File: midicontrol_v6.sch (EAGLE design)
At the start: 67 parts, among them SW1 EC12E_SW, U1 6N138S(TB), U2 PCA9634PW,112, U3 74HC595D, U4 ATMEGA328P-AN, Y1 CSTCE16M0V53-R0

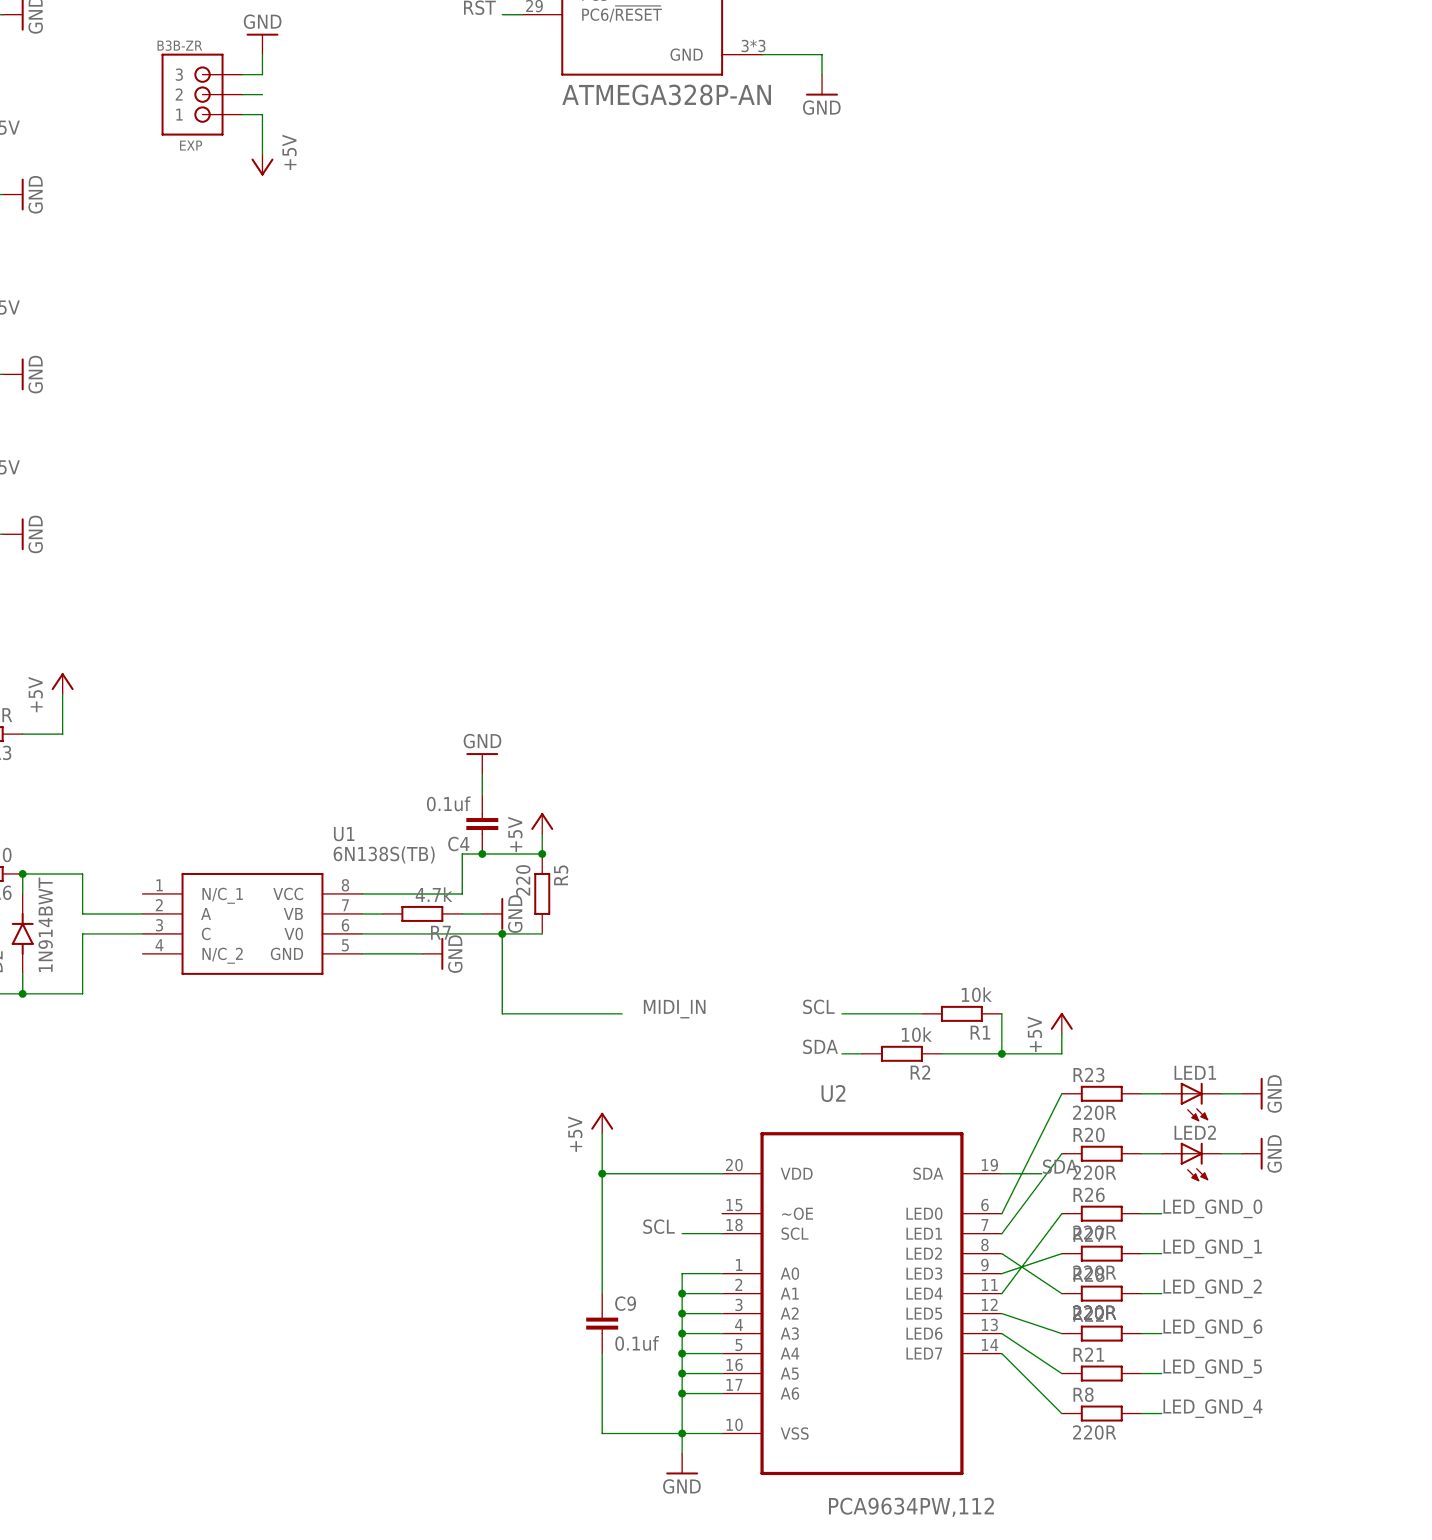
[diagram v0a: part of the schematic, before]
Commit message: finished midiconrol
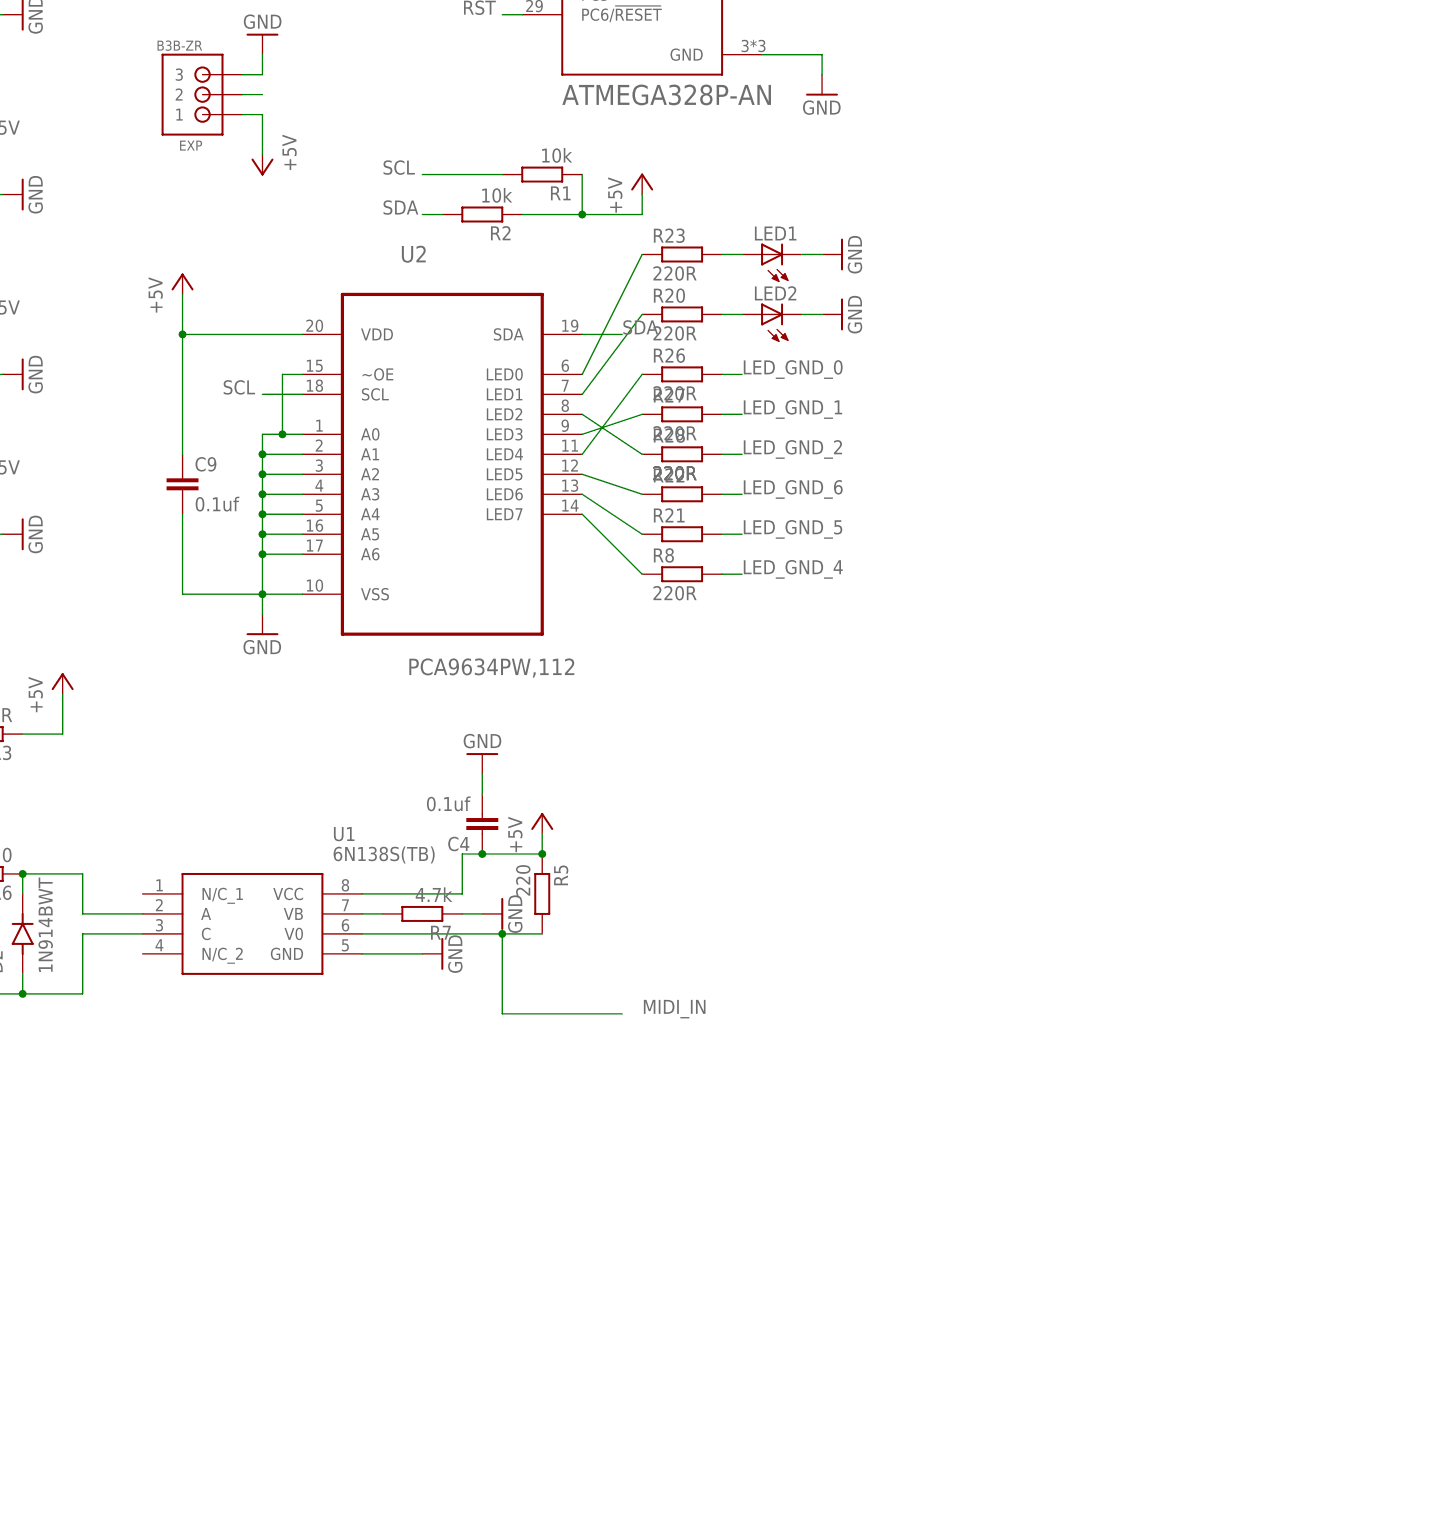
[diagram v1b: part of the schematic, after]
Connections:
- net GND: now also U2.~OE
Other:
- moved on the sheet: C9, LED1, LED2, R1, R2, R20, R21, R22, R23, R26, R27, R28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

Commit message: finalized it
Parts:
- added TP1, TP2, TP3: TPSQTP18R, testpad:TPSQTP18R
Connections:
- net B3: now also TP1.TP
- net B4: now also TP2.TP
- net GND: now also TP3.TP
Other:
- moved on the sheet: C1, C2, C3, C5, CN1, D4, D5, DIS1, IC4, PWR_IN, R34, R35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

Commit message: changed xh to ph pins
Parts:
- removed BTN_0, BTN_1, BTN_2, BTN_3, BTN_4, BTN_5: B3B-ZR, jst:B3B-ZR
- added BTN0, BTN1, BTN2, BTN3, BTN4, BTN5: B3B-PH-K, con-jst-ph:B3B-PH-K
- EXP: value B3B-ZR -> B3B-PH-K; device jst:B3B-ZR -> con-jst-ph:B3B-PH-K
- R35: value 69k -> 125k
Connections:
- net +5V: now also BTN0.2, BTN1.2, BTN2.2, BTN3.2, BTN4.2, BTN5.2; no longer BTN_0.2, BTN_1.2, BTN_2.2, BTN_3.2, BTN_4.2, BTN_5.2
- net B1: now also BTN0.1; no longer BTN_0.1
- net B2: now also BTN1.1; no longer BTN_1.1
- net B3: now also BTN3.1; no longer BTN_3.1
- net B4: now also BTN4.1; no longer BTN_4.1
- net B5: now also BTN5.1; no longer BTN_5.1
- net LED_GND_0: now also BTN2.3; no longer BTN_2.3
- net LED_GND_1: now also BTN1.3; no longer BTN_1.3
- net LED_GND_2: now also BTN0.3; no longer BTN_0.3
- net LED_GND_4: now also BTN5.3; no longer BTN_5.3
- net LED_GND_5: now also BTN4.3; no longer BTN_4.3
- net LED_GND_6: now also BTN3.3; no longer BTN_3.3
- net MISO: now also BTN2.1; no longer BTN_2.1
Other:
- moved on the sheet: EXP
